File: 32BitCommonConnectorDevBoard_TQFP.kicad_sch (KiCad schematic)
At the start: 26 parts, among them J1 Conn_01x06, J2 Conn_02x32_Counter_Clockwise, J3 AVR-ISP-6, SW1 SW_Push, U1 LD1117V33, U2 ATmega1281-16A, Y1 Crystal

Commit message: Rename the schematic pins to reflect port ids
The EBI layout is implied by the design
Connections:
- net CLKO renamed PE7
- net EBI_A10 renamed PC2
- net EBI_A11 renamed PC3
- net EBI_A12 renamed PC4
- net EBI_A13 renamed PC5
- net EBI_A14 renamed PC6
- net EBI_A15 renamed PB7
- net EBI_A16 renamed PG3
- net EBI_A17 renamed PG4
- net EBI_A18 renamed PD2
- net PD2: now also J2.23 (Pin_23); no longer J2.28 (Pin_28)
- net EBI_A19 renamed PD3
- net PD3: now also J2.24 (Pin_24); no longer J2.27 (Pin_27)
- net EBI_A20 renamed PD4
- net PD4: now also J2.25 (Pin_25); no longer J2.26 (Pin_26)
- net EBI_A21 renamed PD5
- net PD5: now also J2.26 (Pin_26); no longer J2.25 (Pin_25)
- net EBI_A22 renamed PD6
- net PD6: now also J2.27 (Pin_27); no longer J2.24 (Pin_24)
- net EBI_A23 renamed PD7
- net PD7: now also J2.28 (Pin_28); no longer J2.23 (Pin_23)
- net EBI_A24 renamed PF0
- net EBI_A25 renamed PF1
- net EBI_A26 renamed PF2
- net EBI_A27 renamed PF3
- net EBI_A28 renamed PF4
- net EBI_A29 renamed PF5
- net EBI_A30 renamed PF6
- net EBI_A31 renamed PF7
- net EBI_A8 renamed PC0
- net EBI_A9 renamed PC1
- net EBI_AD0 renamed PA0
- net EBI_AD1 renamed PA1
- net EBI_AD2 renamed PA2
- net EBI_AD3 renamed PA3
- net EBI_AD4 renamed PA4
- net EBI_AD5 renamed PA5
- net EBI_AD6 renamed PA6
- net EBI_AD7 renamed PA7
- net EBI_ALE renamed PG2
- net ~{CACHE}/BUS renamed PC7
- net ~{EBI_RD} renamed PG1
- net ~{EBI_WR} renamed PG0
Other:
- note added: "CLKO"
- note added: "EBI_A10"
- note added: "EBI_A11"
- note added: "EBI_A12"
- note added: "EBI_A13"
- note added: "EBI_A14"
- note added: "EBI_A15"
- note added: "EBI_A16"
- note added: "EBI_A17"
- note added: "EBI_A18"
- note added: "EBI_A19"
- note added: "EBI_A20"
- note added: "EBI_A21"
- note added: "EBI_A22"
- note added: "EBI_A23"
- note added: "EBI_A24"
- note added: "EBI_A25"
- note added: "EBI_A26"
- note added: "EBI_A27"
- note added: "EBI_A28"
- note added: "EBI_A29"
- note added: "EBI_A30"
- note added: "EBI_A31"
- note added: "EBI_A8"
- note added: "EBI_A9"
- note added: "EBI_AD0"
- note added: "EBI_AD1"
- note added: "EBI_AD2"
- note added: "EBI_AD3"
- note added: "EBI_AD4"
- note added: "EBI_AD5"
- note added: "EBI_AD6"
- note added: "EBI_AD7"
- note added: "EBI_ALE"
- note added: "~{CACHE}/BUS"
- note added: "~{EBI_RD}"
- note added: "~{EBI_WR}"

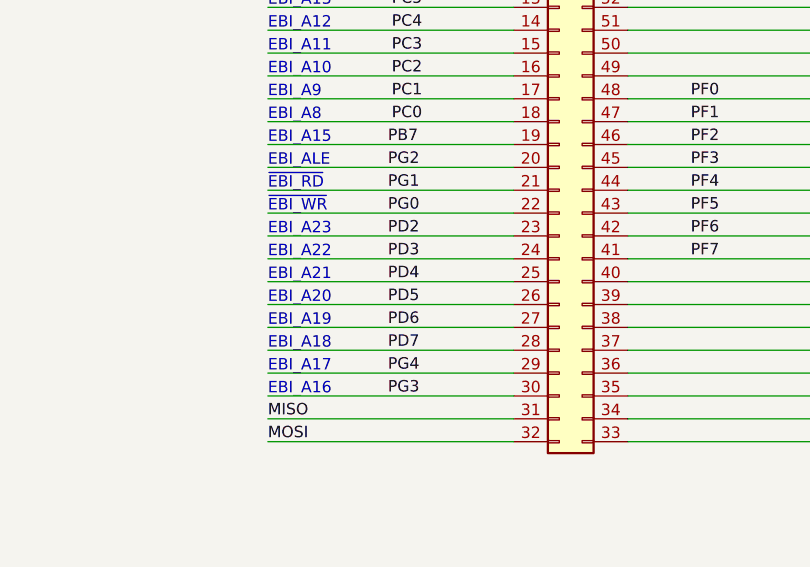
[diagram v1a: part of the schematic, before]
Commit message: Clean up layouts and shrink board slightly
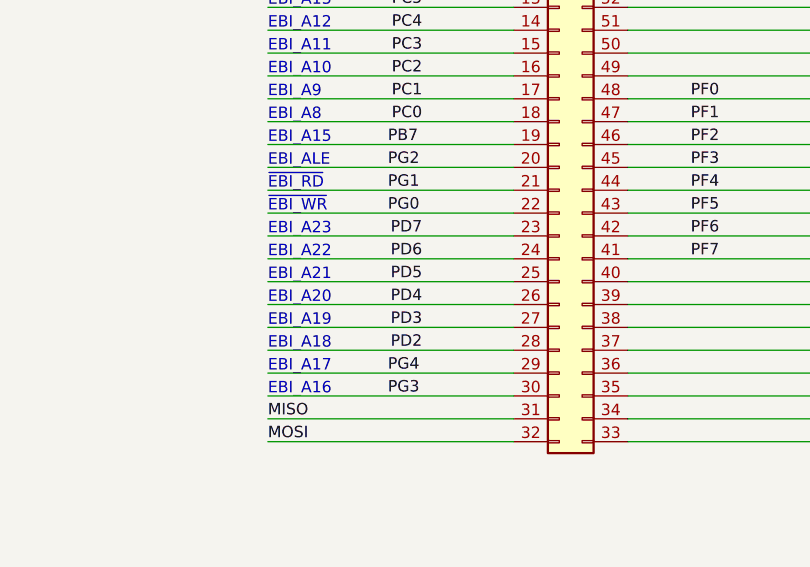
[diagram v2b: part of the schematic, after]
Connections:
- net PD2: now also J2.28 (Pin_28); no longer J2.23 (Pin_23)
- net PD3: now also J2.27 (Pin_27); no longer J2.24 (Pin_24)
- net PD4: now also J2.26 (Pin_26); no longer J2.25 (Pin_25)
- net PD5: now also J2.25 (Pin_25); no longer J2.26 (Pin_26)
- net PD6: now also J2.24 (Pin_24); no longer J2.27 (Pin_27)
- net PD7: now also J2.23 (Pin_23); no longer J2.28 (Pin_28)
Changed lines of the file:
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@@
     (effects (font (size 1.27 1.27)) (justify left bottom))
   )
-  (label "PD7" (at 185.42 175.895 0)
-    (effects (font (size 1.27 1.27)) (justify left bottom))
+  (label "PD7" (at 189.23 163.195 180)
+    (effects (font (size 1.27 1.27)) (justify right bottom))
   )
   (label "PF4" (at 45.085 95.885 0)
@@
     (effects (font (size 1.27 1.27)) (justify left bottom))
   )
-  (label "PD6" (at 185.42 173.355 0)
-    (effects (font (size 1.27 1.27)) (justify left bottom))
+  (label "PD6" (at 189.23 165.735 180)
+    (effects (font (size 1.27 1.27)) (justify right bottom))
   )
   (label "PE4" (at 239.395 135.255 180)
     (effects (font (size 1.27 1.27)) (justify right bottom))
   )
-  (label "PD2" (at 185.42 163.195 0)
-    (effects (font (size 1.27 1.27)) (justify left bottom))
+  (label "PD2" (at 189.23 175.895 180)
+    (effects (font (size 1.27 1.27)) (justify right bottom))
   )
   (label "SDA" (at 239.395 114.935 180)
@@
     (effects (font (size 1.27 1.27)) (justify right bottom))
   )
-  (label "PD5" (at 185.42 170.815 0)
-    (effects (font (size 1.27 1.27)) (justify left bottom))
+  (label "PD5" (at 189.23 168.275 180)
+    (effects (font (size 1.27 1.27)) (justify right bottom))
   )
   (label "PE4" (at 45.085 118.745 0)
@@
     (effects (font (size 1.27 1.27)) (justify left bottom))
   )
-  (label "PD3" (at 185.42 165.735 0)
-    (effects (font (size 1.27 1.27)) (justify left bottom))
+  (label "PD3" (at 189.23 173.355 180)
+    (effects (font (size 1.27 1.27)) (justify right bottom))
   )
   (label "PF0" (at 219.075 147.955 0)
@@
     (effects (font (size 1.27 1.27)) (justify left bottom))
   )
-  (label "PD4" (at 185.42 168.275 0)
-    (effects (font (size 1.27 1.27)) (justify left bottom))
+  (label "PD4" (at 189.23 170.815 180)
+    (effects (font (size 1.27 1.27)) (justify right bottom))
   )
   (label "SDA" (at 130.175 111.125 180)

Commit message: Move PE7 to position 39 on the connector
PG5 is now in place of PB7

Rearrange left over port B so it is:

59 -> PB7
58 -> PB6
57 -> PB5
56 -> PB4

This change allows for the CLKO pin to always be in a non awkward
location
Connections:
- net PB4: now also J2.56 (Pin_56); no longer J2.57 (Pin_57)
- net PB5: now also J2.57 (Pin_57); no longer J2.58 (Pin_58)
- net PB6: now also J2.58 (Pin_58); no longer J2.59 (Pin_59)
- net PB7: now also J2.59 (Pin_59); no longer J2.19 (Pin_19)
- net PE7: now also J2.39 (Pin_39); no longer J2.56 (Pin_56)
- net PG5: now also J2.19 (Pin_19); no longer J2.39 (Pin_39)
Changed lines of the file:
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@@
     (effects (font (size 1.27 1.27)) (justify right bottom))
   )
-  (text "CLKO" (at 239.395 127.635 180)
-    (effects (font (size 1.27 1.27)) (justify right bottom))
+  (text "CLKO" (at 219.075 170.815 0)
+    (effects (font (size 1.27 1.27)) (justify left bottom))
   )
   (text "EBI_A21" (at 113.665 121.285 180)
@@
     (effects (font (size 1.27 1.27)) (justify left bottom))
   )
-  (text "EBI_A15" (at 113.665 80.645 0)
+  (text "EBI_A15" (at 59.69 75.565 0)
     (effects (font (size 1.27 1.27)) (justify left bottom))
   )
@@
     (effects (font (size 1.27 1.27)) (justify right bottom))
   )
-  (label "PB4" (at 239.395 125.095 180)
+  (label "PB4" (at 239.395 127.635 180)
     (effects (font (size 1.27 1.27)) (justify right bottom))
   )
@@
     (effects (font (size 1.27 1.27)) (justify left bottom))
   )
-  (label "PE7" (at 219.075 127.635 0)
-    (effects (font (size 1.27 1.27)) (justify left bottom))
+  (label "PE7" (at 239.395 170.815 180)
+    (effects (font (size 1.27 1.27)) (justify right bottom))
   )
   (label "PG1" (at 45.085 65.405 0)
@@
     (effects (font (size 1.27 1.27)) (justify left bottom))
   )
-  (label "PB5" (at 239.395 122.555 180)
+  (label "PB5" (at 239.395 125.095 180)
     (effects (font (size 1.27 1.27)) (justify right bottom))
   )
@@
     (effects (font (size 1.27 1.27)) (justify left bottom))
   )
-  (label "PG5" (at 239.395 170.815 180)
-    (effects (font (size 1.27 1.27)) (justify right bottom))
+  (label "PG5" (at 185.42 153.035 0)
+    (effects (font (size 1.27 1.27)) (justify left bottom))
   )
   (label "TX0" (at 85.725 243.84 0)
@@
     (effects (font (size 1.27 1.27)) (justify left bottom))
   )
-  (label "PB6" (at 239.395 120.015 180)
+  (label "PB6" (at 239.395 122.555 180)
     (effects (font (size 1.27 1.27)) (justify right bottom))
   )
@@
     (effects (font (size 1.27 1.27)) (justify left bottom))
   )
-  (label "PB7" (at 185.42 153.035 0)
-    (effects (font (size 1.27 1.27)) (justify left bottom))
+  (label "PB7" (at 239.395 120.015 180)
+    (effects (font (size 1.27 1.27)) (justify right bottom))
   )
   (label "AREF" (at 53.34 55.245 0)
